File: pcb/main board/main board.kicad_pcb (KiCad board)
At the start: 2 copper layers, 48 x 22 mm, 65 parts, among them J1 Motor 0 Conn, J10 12V Battery, J11 BAU, J12 Servo 4 Conn, J13 Servo 1 Conn, J14 Servo 2 Conn, J15 Servo 3 Conn, J16 Servo 5 Conn, J17 Servo 6 Conn, J2 Motor 1 Conn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

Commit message: Finished DC motors wiring aand started 5VP regulator.
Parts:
- C14: footprint Capacitor_THT:CP_Radial_D10.0mm_P5.00mm -> Capacitor_THT:CP_Radial_D6.3mm_P2.50mm
- C15, C16, C17: footprint Capacitor_THT:CP_Radial_D10.0mm_P5.00mm -> Capacitor_THT:CP_Radial_D5.0mm_P2.50mm
- moved D11 261.4 mm to (380.0, 66.4), turned to -90 degrees
- moved J3 261.0 mm to (389.0, 76.6), turned to 180 degrees
- moved D15 260.3 mm to (380.0, 87.1), turned to -90 degrees
- moved J4 259.8 mm to (389.0, 89.6), turned to 180 degrees
- moved D12 256.5 mm to (373.5, 66.4), turned to -90 degrees
- moved D16 255.4 mm to (373.5, 87.1), turned to -90 degrees
- moved D9 246.4 mm to (367.0, 66.4), turned to -90 degrees
- moved D13 245.4 mm to (367.0, 87.1), turned to -90 degrees
- moved D10 241.5 mm to (360.5, 66.4), turned to -90 degrees
- moved D14 240.4 mm to (360.5, 87.1), turned to -90 degrees
- moved C15 237.0 mm to (387.0, 99.5), turned to -90 degrees
- moved C16 234.4 mm to (387.0, 123.8), turned to -90 degrees
- moved C17 232.4 mm to (387.0, 149.0), turned to -90 degrees
- moved Q1 154.1 mm to (319.5, 163.0)
- moved J5 151.3 mm to (185.0, 50.4)
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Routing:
- net Net-(D10-A): track 0.00 -> 92.8 mm, vias 0 -> 1
- net Net-(D13-K): track 0.00 -> 75.1 mm, vias 0 -> 1
- net Net-(D11-A): track 0.00 -> 66.6 mm, vias 0 -> 1
- net Net-(D12-A): track 0.00 -> 58.4 mm, vias 0 -> 1
- net Net-(D2-A): track 36.6 -> 92.8 mm, vias 0 -> 1
- net Net-(D4-A): track 47.4 -> 58.7 mm, vias 0 -> 1
- net Net-(D1-A): track 64.6 -> 75.1 mm, vias 0 -> 1
- net Net-(D3-A): track 56.4 -> 66.7 mm, vias 0 -> 1
- net Net-(A5-2B): track 0.00 -> 8.66 mm
- net Net-(A5-2A): track 0.00 -> 8.66 mm
- net Net-(A5-1B): track 0.00 -> 8.66 mm
- net Net-(A5-1A): track 0.00 -> 8.66 mm
- net Net-(A4-2B): track 0.00 -> 8.66 mm
- net Net-(A4-2A): track 0.00 -> 8.66 mm
- net Net-(A4-1B): track 0.00 -> 8.66 mm
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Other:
- board size 48 x 22 mm -> 286.1 x 150.4 mm

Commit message: Rearanged board
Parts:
- added J18: Servo 7 Conn, Connector_PinHeader_2.54mm:PinHeader_1x03_P2.54mm_Vertical, F.Cu at (215.5, 74.0)
- added J19: Servo 8 Conn, Connector_PinHeader_2.54mm:PinHeader_1x03_P2.54mm_Vertical, F.Cu at (224.9, 73.4)
- moved C13 299.8 mm to (63.5, 241.0), turned to 90 degrees
- moved L2 287.7 mm to (73.5, 239.0), turned to -90 degrees
- moved C8 286.2 mm to (63.5, 231.0), turned to 90 degrees
- moved R3 285.4 mm to (66.5, 231.0), turned to -90 degrees
- moved C14 278.0 mm to (85.5, 238.0), turned to -90 degrees
- moved R4 273.0 mm to (80.5, 231.0), turned to -90 degrees
- moved C9 268.0 mm to (83.5, 231.0)
- moved R2 266.6 mm to (86.5, 234.7), turned to 90 degrees
- moved U6 262.8 mm to (73.5, 225.0), turned to 90 degrees
- moved R1 259.8 mm to (83.0, 223.0)
- moved Q1 255.2 mm to (70.0, 216.5), turned to -90 degrees
- moved Q2 250.0 mm to (77.0, 216.5), turned to -90 degrees
- moved C7 244.7 mm to (71.0, 210.5), turned to 0 degrees
- moved C10 230.6 mm to (104.0, 208.2), turned to 90 degrees
- moved C11 226.8 mm to (109.5, 208.2), turned to 90 degrees
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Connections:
- A1 pad 14: unconnected-(A1-GPIO10-Pad14) -> Servo 7 PWM
- A1 pad 15: unconnected-(A1-GPIO11-Pad15) -> Servo 8 PWM
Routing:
- net Net-(U6-FB): track 0.00 -> 16.7 mm
- net Net-(U6-RON): track 0.00 -> 13.9 mm
- net Net-(U6-SS): track 0.00 -> 10.7 mm
- net Net-(U6-VCC): track 0.00 -> 9.99 mm
- net GNDPWR: track 0.00 -> 6.53 mm
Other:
- board size 286.1 x 150.4 mm -> 147.9 x 156.6 mm

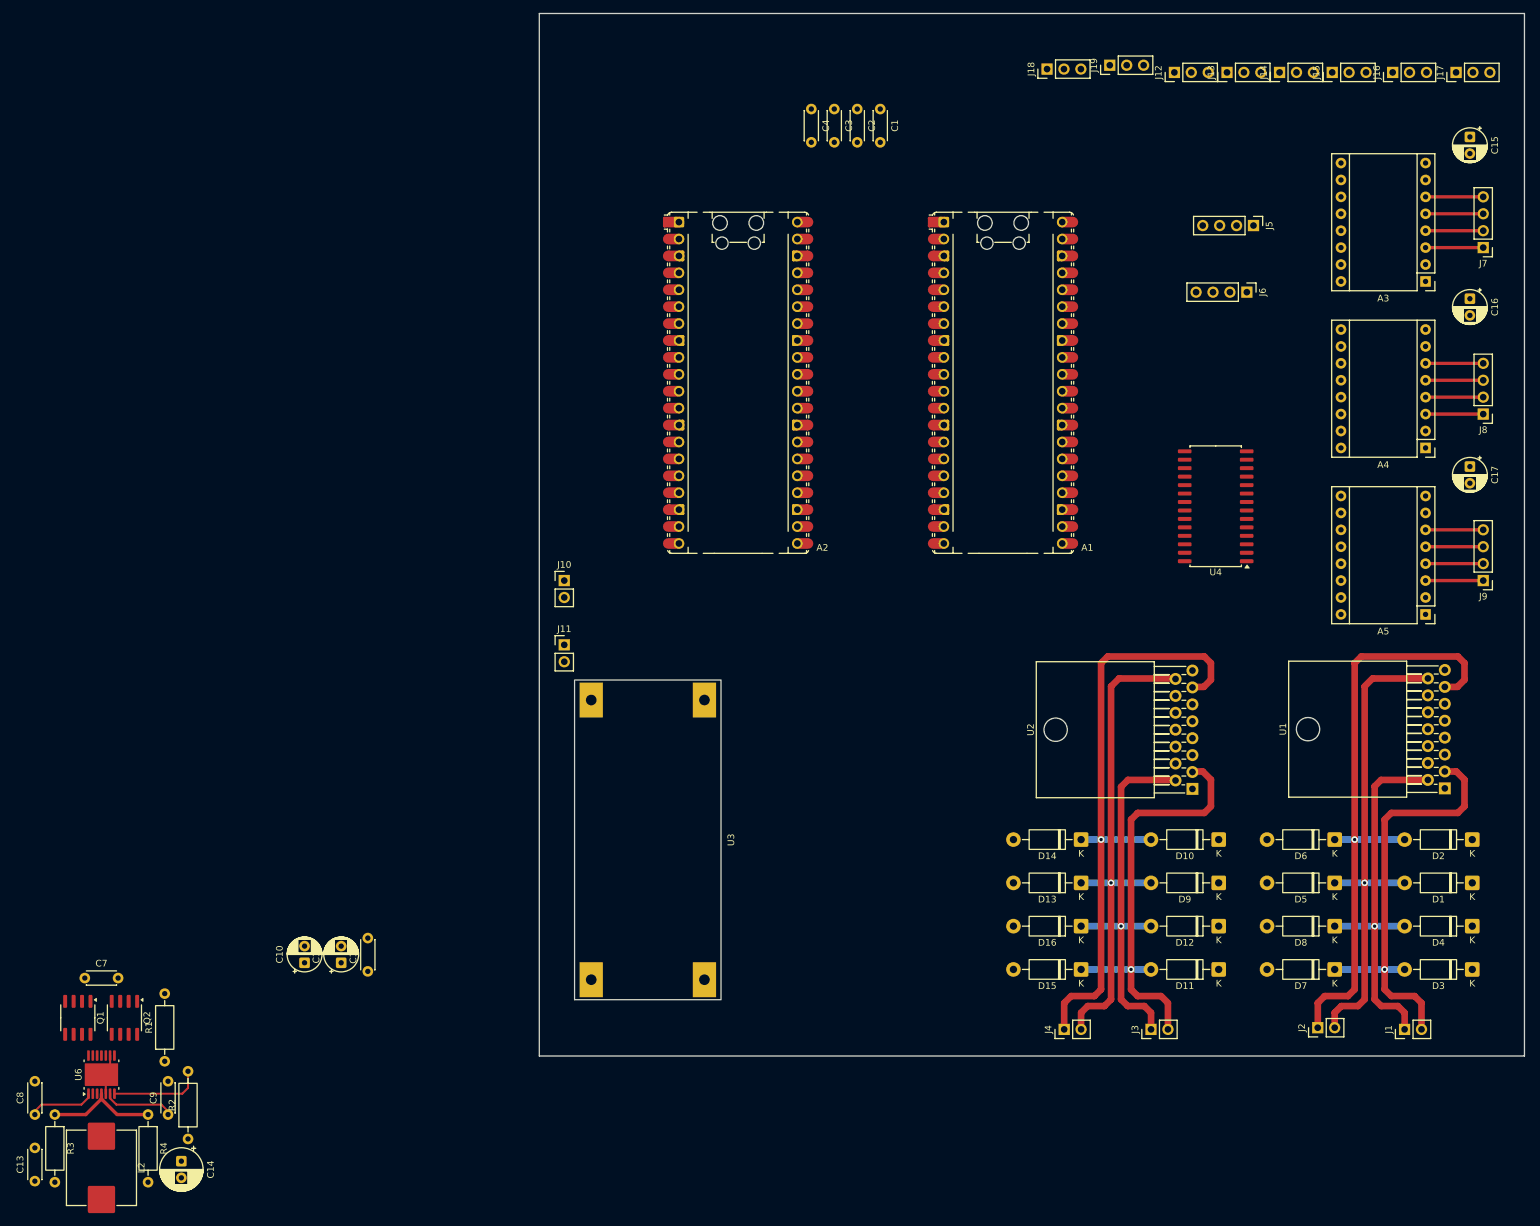
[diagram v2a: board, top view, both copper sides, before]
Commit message: Finished wiring 5VP, created mass plane and started to wire motor drivers.
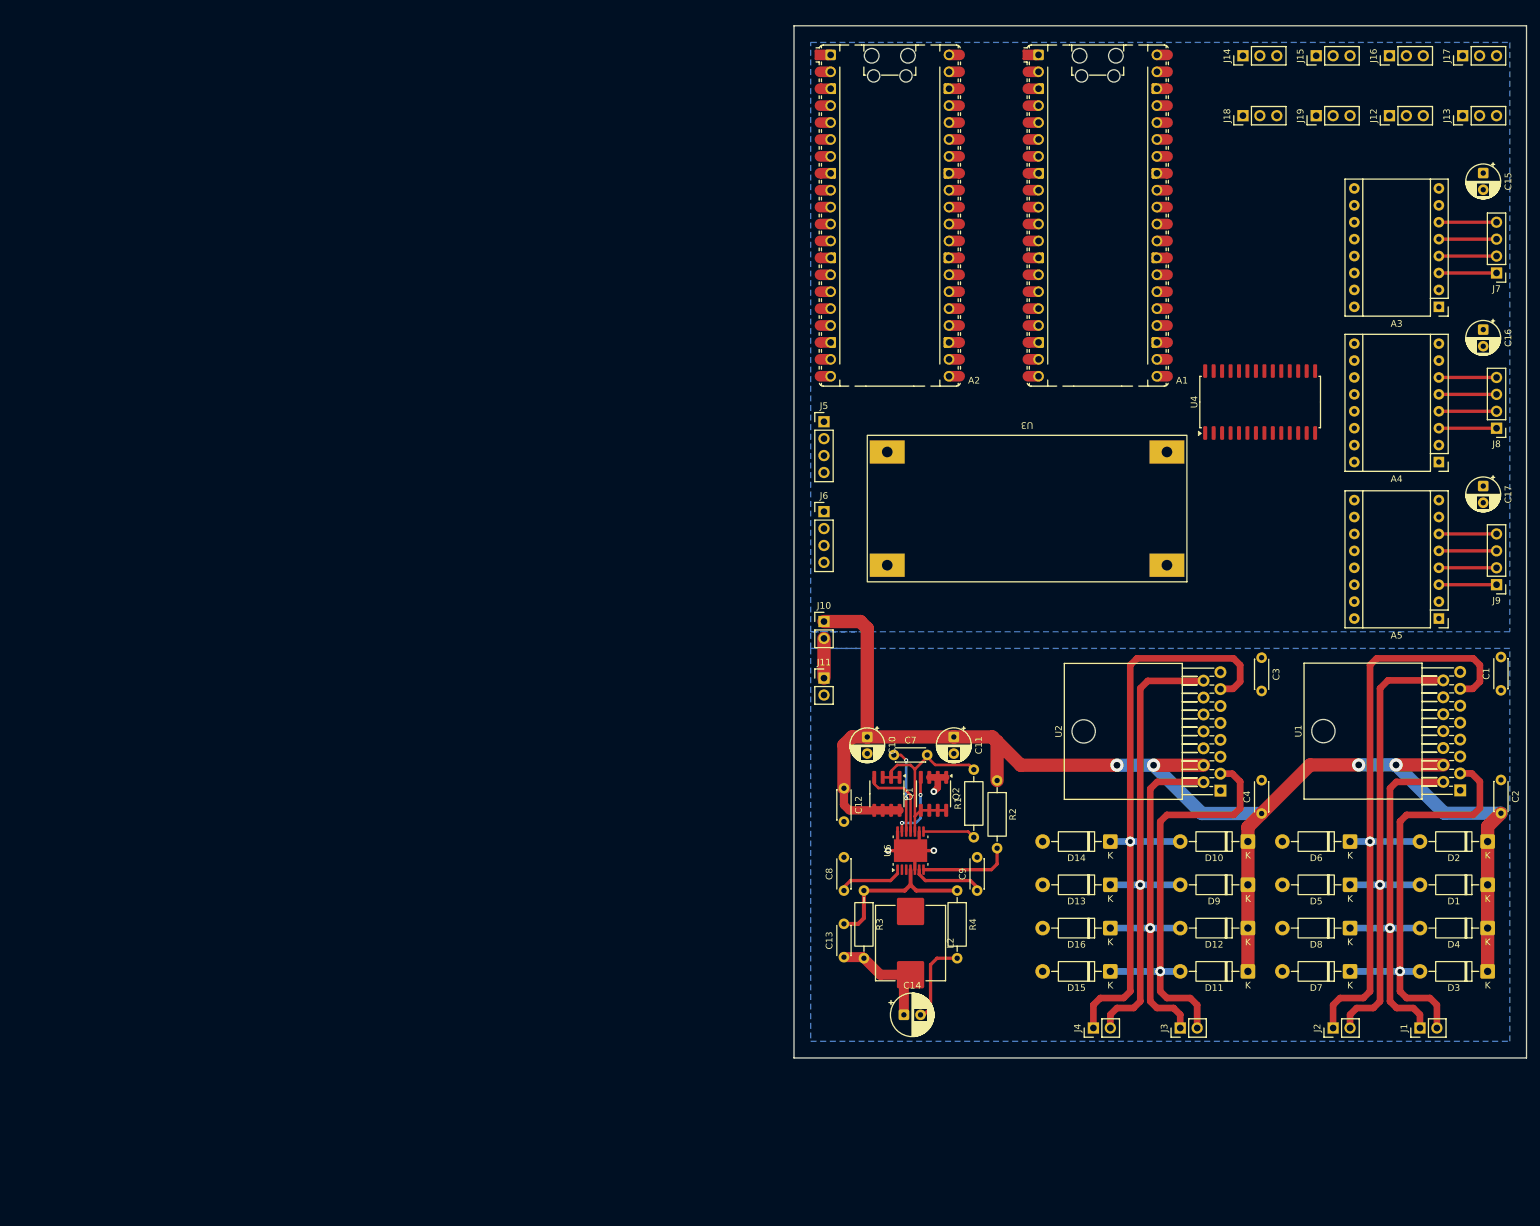
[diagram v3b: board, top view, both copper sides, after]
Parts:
- moved C2 139.6 mm to (283.7, 180.8)
- moved R2 132.9 mm to (208.0, 180.8), turned to -90 degrees
- moved C1 127.7 mm to (283.7, 167.3), turned to 90 degrees
- moved L2 126.1 mm to (195.0, 205.2)
- moved C13 126.1 mm to (185.0, 207.4)
- moved C8 126.1 mm to (185.0, 197.4)
- moved C9 126.1 mm to (205.0, 197.4)
- moved R1 126.1 mm to (204.5, 189.4)
- moved R3 126.1 mm to (188.0, 197.4)
- moved R4 126.1 mm to (202.0, 197.4)
- moved U6 126.1 mm to (195.0, 191.4)
- moved Q1 126.1 mm to (191.4, 182.8)
- moved Q2 126.1 mm to (198.4, 182.8)
- moved C7 126.0 mm to (192.5, 177.0)
- moved C4 125.6 mm to (247.7, 185.8), turned to 90 degrees
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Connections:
- U4 pad 1: Motor 1 Direction Pin 1 -> Motor 4 Direction Pin 1
- U4 pad 2: Motor 1 Direction Pin 2 -> Motor 4 Direction Pin 2
- U4 pad 3: Motor 2 Direction Pin 1 -> Motor 3 Direction Pin 1
- U4 pad 4: Motor 2 Direction Pin 2 -> Motor 3 Direction Pin 2
- U4 pad 5: Motor 3 Direction Pin 1 -> Motor 1 Direction Pin 1
- U4 pad 6: Motor 3 Direction Pin 2 -> Motor 1 Direction Pin 2
- U4 pad 7: Motor 4 Direction Pin 1 -> Motor 2 Direction Pin 1
- U4 pad 8: Motor 4 Direction Pin 2 -> Motor 2 Direction Pin 2
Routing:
- net +12V: track 0.00 -> 220.4 mm, vias 0 -> 4
- net Net-(U6-SW): track 0.00 -> 32.8 mm
- net +5VP: track 0.00 -> 17.6 mm
- net GNDPWR: track 6.53 -> 22.4 mm, vias 0 -> 3
- net Net-(U6-BST): track 0.00 -> 12.9 mm, vias 0 -> 2
- net Net-(C14-Pad2): track 0.00 -> 12.8 mm
- net Net-(Q1-G): track 0.00 -> 12.6 mm
- net Net-(Q2-G): track 0.00 -> 10.5 mm, vias 0 -> 2
- net Net-(U6-ILIM): track 0.00 -> 7.91 mm
- net Net-(U6-FB): track 16.7 -> 24.5 mm
- net Net-(J10-Pin_2): track 0.00 -> 5.96 mm
- net Net-(D3-A): track 66.7 -> 66.1 mm
- net Net-(D11-A): track 66.6 -> 66.1 mm
- net Net-(D4-A): track 58.7 -> 58.2 mm
- added copper zone on B.Cu, net GNDPWR
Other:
- board size 147.9 x 156.6 mm -> 110 x 155 mm

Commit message: Continued Conecting motors drivers
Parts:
- moved C15 0.38 mm to (281.0, 90.0)
- moved C16 0.38 mm to (281.0, 113.5)
- moved C17 0.38 mm to (281.0, 137.0)
- moved A4 0.25 mm to (274.5, 133.2)
- moved A5 0.25 mm to (274.5, 156.7)
- moved J8 0.19 mm to (283.0, 128.1)
- moved J9 0.19 mm to (283.0, 151.6)
- moved A3 0.16 mm to (274.5, 109.7)
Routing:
- net +5VL: track 0.00 -> 54.8 mm
- net +12V: track 220.4 -> 261.3 mm, vias 4 -> 6
- net Net-(U6-SW): track 32.8 -> 52.6 mm, vias 0 -> 2
- net Motor 2 Activation Pin: track 0.00 -> 8.71 mm

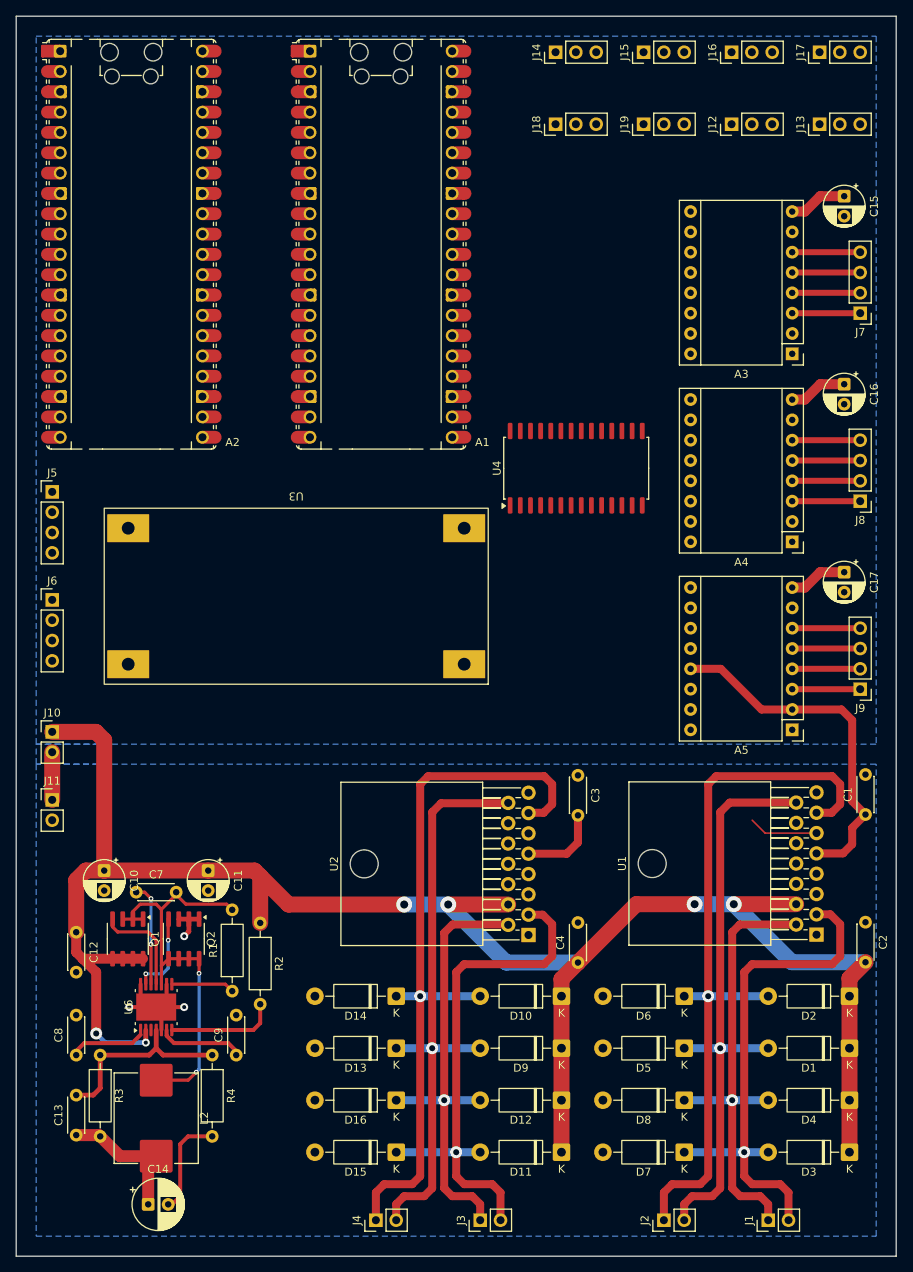
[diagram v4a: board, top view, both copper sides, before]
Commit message: Almost finished wiring motors drivers and continued connecting the rest. Also modified the LM2596S Module to put a hole in the board
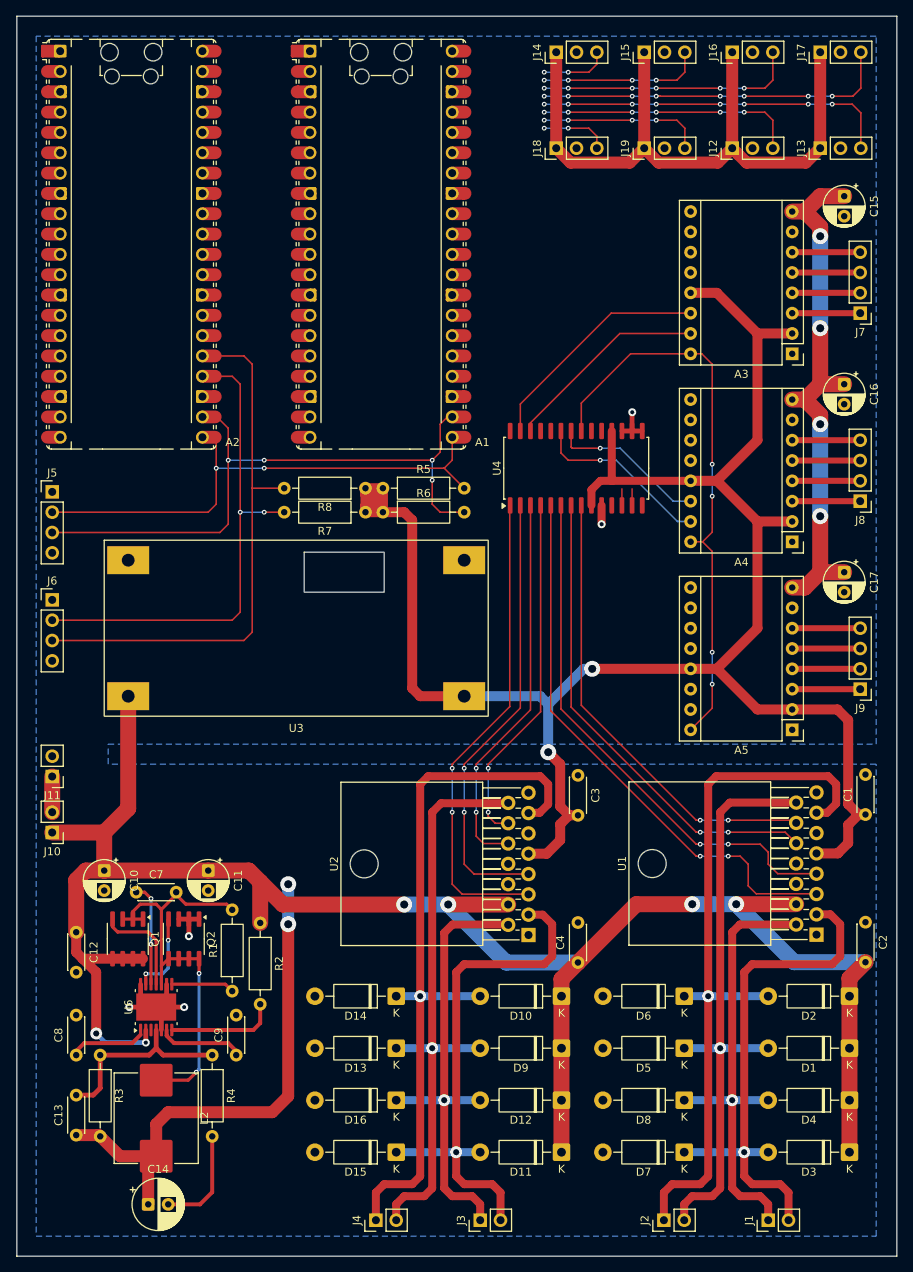
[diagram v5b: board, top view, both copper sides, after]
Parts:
- added R5: 4.7kΩ, Resistor_THT:R_Axial_DIN0207_L6.3mm_D2.5mm_P10.16mm_Horizontal, F.Cu at (223.3, 126.5)
- added R6: 4.7kΩ, Resistor_THT:R_Axial_DIN0207_L6.3mm_D2.5mm_P10.16mm_Horizontal, F.Cu at (223.3, 129.5)
- added R7: 4.7kΩ, Resistor_THT:R_Axial_DIN0207_L6.3mm_D2.5mm_P10.16mm_Horizontal, F.Cu at (221.2, 129.5)
- added R8: 4.7kΩ, Resistor_THT:R_Axial_DIN0207_L6.3mm_D2.5mm_P10.16mm_Horizontal, F.Cu at (221.2, 126.5)
- J7: value Stepper 0 Conn -> Stepper 1 Conn
- J8: value Stepper 1 Conn -> Stepper 2 Conn
- J9: value Stepper 2 Conn -> Stepper 3 Conn
- moved J10 12.6 mm to (182.0, 169.5), turned to 180 degrees
- moved U3 4.00 mm to (212.5, 144.0), turned to 0 degrees
- moved J18 3.00 mm to (245.0, 84.0)
- moved J19 3.00 mm to (256.0, 84.0)
- moved J12 3.00 mm to (267.0, 84.0)
- moved J13 3.00 mm to (278.0, 84.0)
- moved J11 2.92 mm to (182.0, 162.5), turned to 180 degrees
- moved J14 0.08 mm to (245.0, 72.0)
- moved J15 0.08 mm to (256.0, 72.0)
- moved J16 0.08 mm to (267.0, 72.0)
- moved J17 0.08 mm to (278.0, 72.0)
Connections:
- A3 pad 14: Stepper 0 Sleep -> Stepper 1 Sleep
- A3 pad 15: Stepper 0 Step -> Stepper 1 Step
- A4 pad 14: Stepper 1 Sleep -> Stepper 2 Sleep
- A4 pad 15: Stepper 1 Step -> Stepper 2 Step
- A5 pad 14: Stepper 2 Sleep -> Stepper 3 Sleep
- A5 pad 15: Stepper 2 Step -> Stepper 3 Step
- U4 pad 1: Motor 4 Direction Pin 1 -> Motor 3 Direction Pin 1
- U4 pad 2: Motor 4 Direction Pin 2 -> Motor 3 Direction Pin 2
- U4 pad 22: Stepper 0 Sleep -> Stepper 2 Sleep
- U4 pad 23: Stepper 0 Step -> Stepper 2 Step
- U4 pad 24: Stepper 1 Sleep -> Stepper 3 Sleep
- U4 pad 25: Stepper 1 Step -> Stepper 3 Step
- U4 pad 26: Stepper 2 Sleep -> Stepper 1 Step
- U4 pad 27: Stepper 2 Step -> Stepper 1 Sleep
- U4 pad 3: Motor 3 Direction Pin 1 -> Motor 4 Direction Pin 1
- U4 pad 4: Motor 3 Direction Pin 2 -> Motor 4 Direction Pin 2
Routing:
- net +5VL: track 54.8 -> 240.9 mm, vias 0 -> 2
- net +5VP: track 17.6 -> 151.5 mm, vias 0 -> 2
- net I2C 0 SCL: track 0.00 -> 82.5 mm, vias 0 -> 4
- net Steppers Dir: track 0.00 -> 72.3 mm, vias 0 -> 4
- net Motor 1 Direction Pin 1: track 0.00 -> 70.0 mm, vias 0 -> 2
- net I2C 1 SCL: track 0.00 -> 69.6 mm
- net I2C 0 SDA: track 0.00 -> 69.0 mm, vias 0 -> 2
- net Motor 1 Direction Pin 2: track 0.00 -> 66.8 mm, vias 0 -> 2
- net I2C 1 SDA: track 0.00 -> 63.0 mm, vias 0 -> 2
- net Motor 3 Direction Pin 1: track 0.00 -> 60.4 mm, vias 0 -> 2
- net Motor 2 Direction Pin 1: track 0.00 -> 60.4 mm, vias 0 -> 2
- net Motor 2 Direction Pin 2: track 0.00 -> 57.9 mm, vias 0 -> 2
- net Motor 3 Direction Pin 2: track 0.00 -> 56.3 mm, vias 0 -> 2
- net +12V: track 261.3 -> 311.4 mm, vias 6 -> 10
- net Motor 4 Direction Pin 1: track 0.00 -> 48.5 mm, vias 0 -> 2
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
